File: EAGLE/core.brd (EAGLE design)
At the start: 20.3 x 35.6 mm, 47 parts, among them IC1 MCP1825S-3302E, Q1 MMDT3904, U2 STM32F10XCXT6, U3 SST25VF040B-S2, U4 NL17SZ125SOT553, X1 USB-MICROB, X2 IPEX-20279-001E, Y1 32Khz, Y2 8Mhz

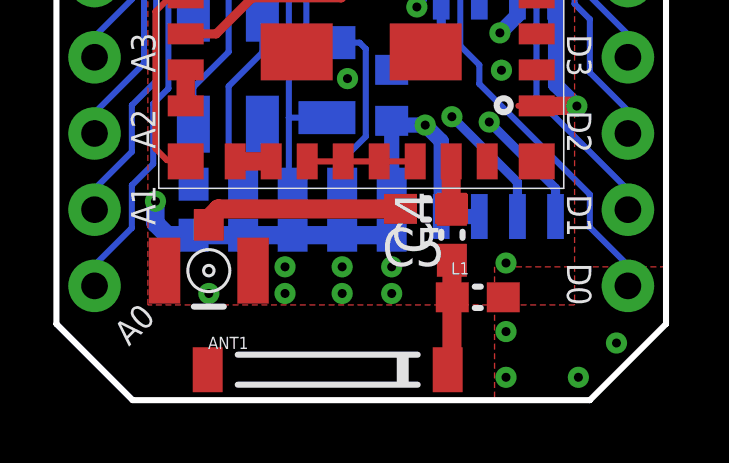
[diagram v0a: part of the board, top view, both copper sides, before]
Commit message: Tweaked schematic and board layout for alternate matching components (parallel then series)
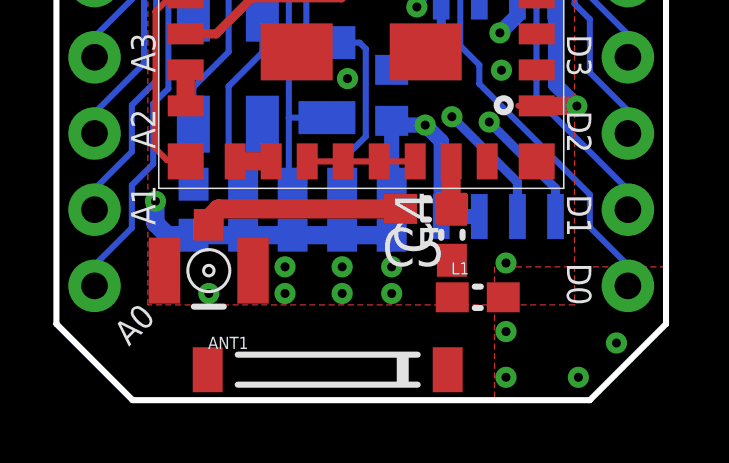
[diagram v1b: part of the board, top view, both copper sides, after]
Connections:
- net N$3: no longer L1.1
- net N$5: now also L1.1
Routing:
- net N$3: track 3.72 -> 0.00 mm
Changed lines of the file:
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@@
 <grid distance="5" unitdist="mil" unit="mil" style="lines" multiple="1" display="yes" altdistance="0.005" altunitdist="inch" altunit="inch"/>
 <layers>
-<layer number="1" name="Top" color="4" fill="1" visible="no" active="yes"/>
+<layer number="1" name="Top" color="4" fill="1" visible="yes" active="yes"/>
 <layer number="2" name="$GND" color="13" fill="1" visible="no" active="yes"/>
 <layer number="3" name="Route3" color="4" fill="3" visible="no" active="no"/>
@@
 <layer number="14" name="Route14" color="1" fill="6" visible="no" active="no"/>
 <layer number="15" name="$+3V3" color="11" fill="1" visible="no" active="yes"/>
-<layer number="16" name="Bottom" color="1" fill="1" visible="no" active="yes"/>
+<layer number="16" name="Bottom" color="1" fill="1" visible="yes" active="yes"/>
 <layer number="17" name="Pads" color="2" fill="1" visible="yes" active="yes"/>
-<layer number="18" name="Vias" color="2" fill="1" visible="no" active="yes"/>
-<layer number="19" name="Unrouted" color="6" fill="1" visible="no" active="yes"/>
+<layer number="18" name="Vias" color="2" fill="1" visible="yes" active="yes"/>
+<layer number="19" name="Unrouted" color="6" fill="1" visible="yes" active="yes"/>
 <layer number="20" name="Dimension" color="6" fill="1" visible="yes" active="yes"/>
 <layer number="21" name="tPlace" color="16" fill="1" visible="yes" active="yes"/>
-<layer number="22" name="bPlace" color="14" fill="1" visible="no" active="yes"/>
+<layer number="22" name="bPlace" color="14" fill="1" visible="yes" active="yes"/>
 <layer number="23" name="tOrigins" color="15" fill="1" visible="yes" active="yes"/>
-<layer number="24" name="bOrigins" color="15" fill="1" visible="no" active="yes"/>
+<layer number="24" name="bOrigins" color="15" fill="1" visible="yes" active="yes"/>
 <layer number="25" name="tNames" color="7" fill="1" visible="no" active="yes"/>
 <layer number="26" name="bNames" color="7" fill="1" visible="no" active="yes"/>
-<layer number="27" name="tValues" color="7" fill="1" visible="yes" active="yes"/>
+<layer number="27" name="tValues" color="7" fill="1" visible="no" active="yes"/>
 <layer number="28" name="bValues" color="7" fill="1" visible="no" active="yes"/>
 <layer number="29" name="tStop" color="7" fill="3" visible="no" active="yes"/>
 <layer number="30" name="bStop" color="7" fill="6" visible="no" active="yes"/>
-<layer number="31" name="tCream" color="7" fill="4" visible="yes" active="yes"/>
+<layer number="31" name="tCream" color="7" fill="4" visible="no" active="yes"/>
 <layer number="32" name="bCream" color="7" fill="5" visible="no" active="yes"/>
 <layer number="33" name="tFinish" color="6" fill="3" visible="no" active="yes"/>
@@
 <wire x1="11.469" y1="6.3754" x2="5.3975" y2="6.3754" width="0.635" layer="1"/>
 </signal>
-<signal name="N$3" class="2">
-<contactref element="ANT1" pad="SIG"/>
-<contactref element="C4" pad="1"/>
-<contactref element="L1" pad="1"/>
-<wire x1="13.1826" y1="4.6618" x2="13.1826" y2="3.4426" width="0.635" layer="1"/>
-<wire x1="13.1826" y1="3.4426" x2="13.1962" y2="3.429" width="0.635" layer="1"/>
-<wire x1="13.1826" y1="3.4426" x2="13.1826" y2="1.1562" width="0.635" layer="1"/>
-<wire x1="13.1826" y1="1.1562" x2="13.0424" y2="1.016" width="0.635" layer="1"/>
-</signal>
 <signal name="N$5" class="2">
 <contactref element="C4" pad="2"/>
@@
 <wire x1="13.16" y1="7.96" x2="13.16" y2="6.3844" width="0.635" layer="1"/>
 <wire x1="13.16" y1="6.3844" x2="13.169" y2="6.3754" width="0.635" layer="1"/>
+<contactref element="L1" pad="1"/>
+<wire x1="13.1962" y1="3.429" x2="13.1826" y2="6.3618" width="0" layer="19" extent="1-1"/>
 </signal>
 <signal name="LED1">
@@
 <wire x1="16.6624" y1="28.9052" x2="16.383" y2="28.6258" width="0.2032" layer="15"/>
 </signal>
+<signal name="N$3">
+<contactref element="C4" pad="1"/>
+<contactref element="ANT1" pad="SIG"/>
+<wire x1="13.0424" y1="1.016" x2="13.1826" y2="4.6618" width="0" layer="19" extent="1-1"/>
+</signal>
 </signals>

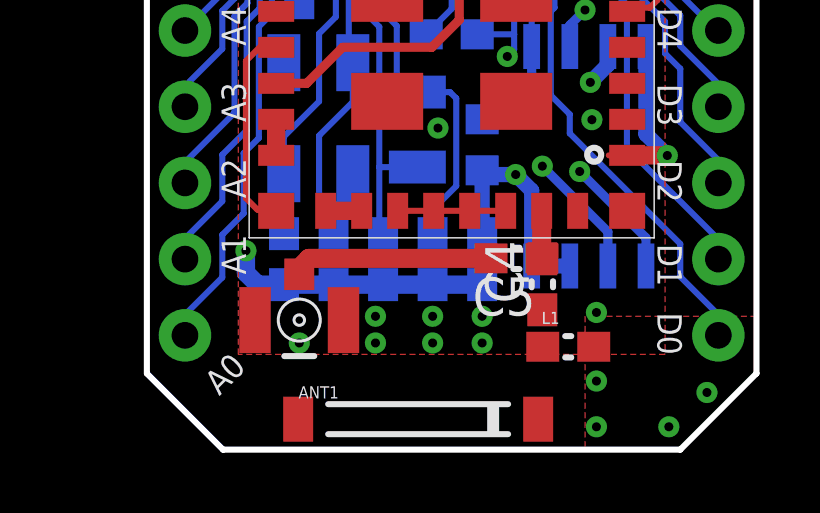
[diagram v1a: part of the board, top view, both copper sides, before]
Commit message: Further layout tweaks
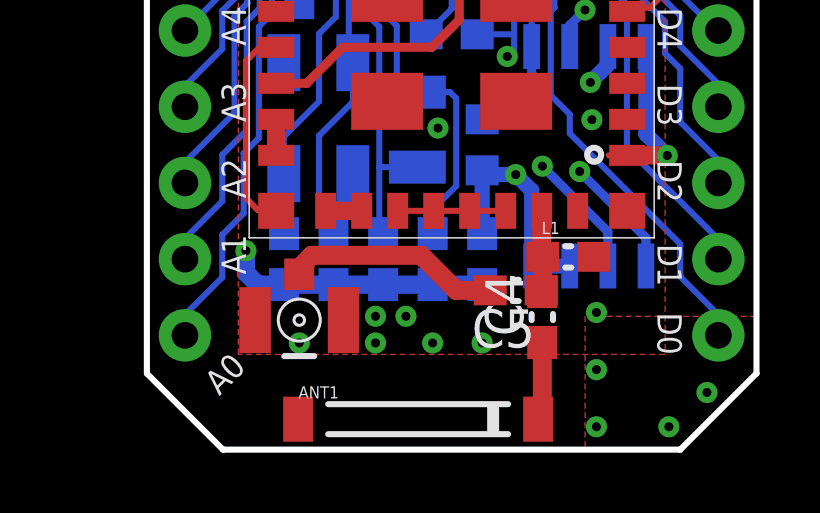
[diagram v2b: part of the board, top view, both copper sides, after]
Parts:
- moved L1 3.00 mm to (14.0, 6.43)
- moved C4 1.09 mm to (13.2, 4.42)
- moved C5 1.07 mm to (12.3, 5.31)
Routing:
- net N$3: track 0.00 -> 2.61 mm
- net N$5: track 1.61 -> 2.74 mm
- net N$2: track 6.73 -> 7.23 mm
- net GND: vias 27 -> 26
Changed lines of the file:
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@@
 </element>
 <element name="U1" library="CC3000" package="CC3000" value="" x="10.16" y="15.24" locked="yes" smashed="yes" rot="R180"/>
-<element name="C4" library="rcl" package="C0603" value="2.2pF" x="13.1826" y="5.5118" smashed="yes" rot="R90">
-<attribute name="NAME" x="12.5476" y="4.8768" size="1.27" layer="25" rot="R90"/>
-<attribute name="VALUE" x="12.5476" y="5.0292" size="0.4064" layer="27" rot="R180"/>
+<element name="C4" library="rcl" package="C0603" value="2.2pF" x="13.1826" y="4.4196" smashed="yes" rot="R90">
+<attribute name="NAME" x="12.5476" y="3.7846" size="1.27" layer="25" rot="R90"/>
+<attribute name="VALUE" x="12.5476" y="3.937" size="0.4064" layer="27" rot="R180"/>
 </element>
 <element name="C3" library="rcl" package="C0603" value="100nF" x="5.969" y="24.257" locked="yes" smashed="yes">
@@
 </element>
 <element name="X2" library="Spark" package="IPEX-20279-001E" value="IPEX-20279-001E" x="5.08" y="4.318" locked="yes"/>
-<element name="C5" library="rcl" package="C0603" value="10pF" x="12.319" y="6.3754" smashed="yes" rot="R180">
-<attribute name="NAME" x="12.954" y="5.7404" size="1.27" layer="25" rot="R180"/>
-<attribute name="VALUE" x="10.668" y="6.5024" size="0.4064" layer="27" rot="R180"/>
+<element name="C5" library="rcl" package="C0603" value="10pF" x="12.2936" y="5.3086" smashed="yes" rot="R180">
+<attribute name="NAME" x="12.9286" y="4.6736" size="1.27" layer="25" rot="R180"/>
+<attribute name="VALUE" x="10.6426" y="5.4356" size="0.4064" layer="27" rot="R180"/>
 </element>
 <element name="ANT1" library="Spark" package="AT8010" value="AT8010" x="9.0424" y="1.016" smashed="yes">
@@
 </element>
 <element name="D1" library="Spark" package="DIODE-DO-220AA(SMP)" value="DIODE" x="3.048" y="34.036" locked="yes"/>
-<element name="L1" library="SparkFun-Passives" package="0603" value="2.2nH" x="14.0462" y="3.429"/>
+<element name="L1" library="SparkFun-Passives" package="0603" value="2.2nH" x="14.0462" y="6.4262"/>
 <element name="U4" library="Spark" package="SOT-553" value="NL17SZ125SOT553" x="15.6718" y="29.21" rot="MR270"/>
 </elements>
@@
 <via x="0.9144" y="33.3248" extent="1-16" drill="0.3"/>
 <contactref element="L1" pad="2"/>
-<via x="14.986" y="2.286" extent="1-16" drill="0.3"/>
-<via x="11.176" y="4.445" extent="1-16" drill="0.3"/>
+<via x="14.986" y="2.667" extent="1-16" drill="0.3"/>
 <via x="14.986" y="4.572" extent="1-16" drill="0.3"/>
 <contactref element="U1" pad="GND@11"/>
@@
 <vertex x="20.32" y="4.445"/>
 </polygon>
-<via x="9.525" y="4.445" extent="1-16" drill="0.3"/>
+<via x="8.636" y="4.445" extent="1-16" drill="0.3"/>
 <via x="7.62" y="4.445" extent="1-16" drill="0.3"/>
 <via x="14.986" y="0.762" extent="1-16" drill="0.3"/>
@@
 <contactref element="C5" pad="2"/>
 <contactref element="X2" pad="1"/>
-<wire x1="5.3975" y1="6.3754" x2="5.08" y2="6.0579" width="0.635" layer="1"/>
+<wire x1="5.4991" y1="6.477" x2="5.08" y2="6.0579" width="0.635" layer="1"/>
 <wire x1="5.08" y1="6.0579" x2="5.08" y2="5.8455" width="0.635" layer="1"/>
-<wire x1="11.469" y1="6.3754" x2="5.3975" y2="6.3754" width="0.635" layer="1"/>
+<wire x1="11.4436" y1="5.3086" x2="10.3124" y2="5.3086" width="0.635" layer="1"/>
+<wire x1="10.3124" y1="5.3086" x2="9.144" y2="6.477" width="0.635" layer="1"/>
+<wire x1="9.144" y1="6.477" x2="5.4991" y2="6.477" width="0.635" layer="1"/>
 </signal>
 <signal name="N$5" class="2">
@@
 <contactref element="U1" pad="RF_ANT"/>
 <contactref element="C5" pad="1"/>
-<wire x1="13.1826" y1="6.3618" x2="13.169" y2="6.3754" width="0.635" layer="1"/>
-<wire x1="13.16" y1="7.96" x2="13.16" y2="6.3844" width="0.635" layer="1"/>
-<wire x1="13.16" y1="6.3844" x2="13.169" y2="6.3754" width="0.635" layer="1"/>
+<wire x1="13.1826" y1="5.2696" x2="13.1436" y2="5.3086" width="0.635" layer="1"/>
 <contactref element="L1" pad="1"/>
-<wire x1="13.1962" y1="3.429" x2="13.1826" y2="6.3618" width="0" layer="19" extent="1-1"/>
+<wire x1="13.16" y1="7.96" x2="13.16" y2="6.4624" width="0.635" layer="1"/>
+<wire x1="13.16" y1="6.4624" x2="13.1962" y2="6.4262" width="0.635" layer="1"/>
+<wire x1="13.1962" y1="6.4262" x2="13.1962" y2="5.3612" width="0.635" layer="1"/>
+<wire x1="13.1962" y1="5.3612" x2="13.1436" y2="5.3086" width="0.635" layer="1"/>
 </signal>
 <signal name="LED1">
@@
 <wire x1="16.6624" y1="28.9052" x2="16.383" y2="28.6258" width="0.2032" layer="15"/>
 </signal>
-<signal name="N$3">
+<signal name="N$3" class="2">
 <contactref element="C4" pad="1"/>
 <contactref element="ANT1" pad="SIG"/>
-<wire x1="13.0424" y1="1.016" x2="13.1826" y2="4.6618" width="0" layer="19" extent="1-1"/>
+<wire x1="13.1826" y1="3.5696" x2="13.1826" y2="1.1562" width="0.635" layer="1"/>
+<wire x1="13.1826" y1="1.1562" x2="13.0424" y2="1.016" width="0.635" layer="1"/>
 </signal>
 </signals>
